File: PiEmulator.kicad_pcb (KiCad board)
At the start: 2 copper layers, 180 x 60 mm, 45 parts, among them J1 Conn_01x01, J2 Conn_01x01, J3 USB_C_Receptacle_USB2.0, U1 ADA3708, U3 BQ24090DGQ, U4 TPS61230DRCR

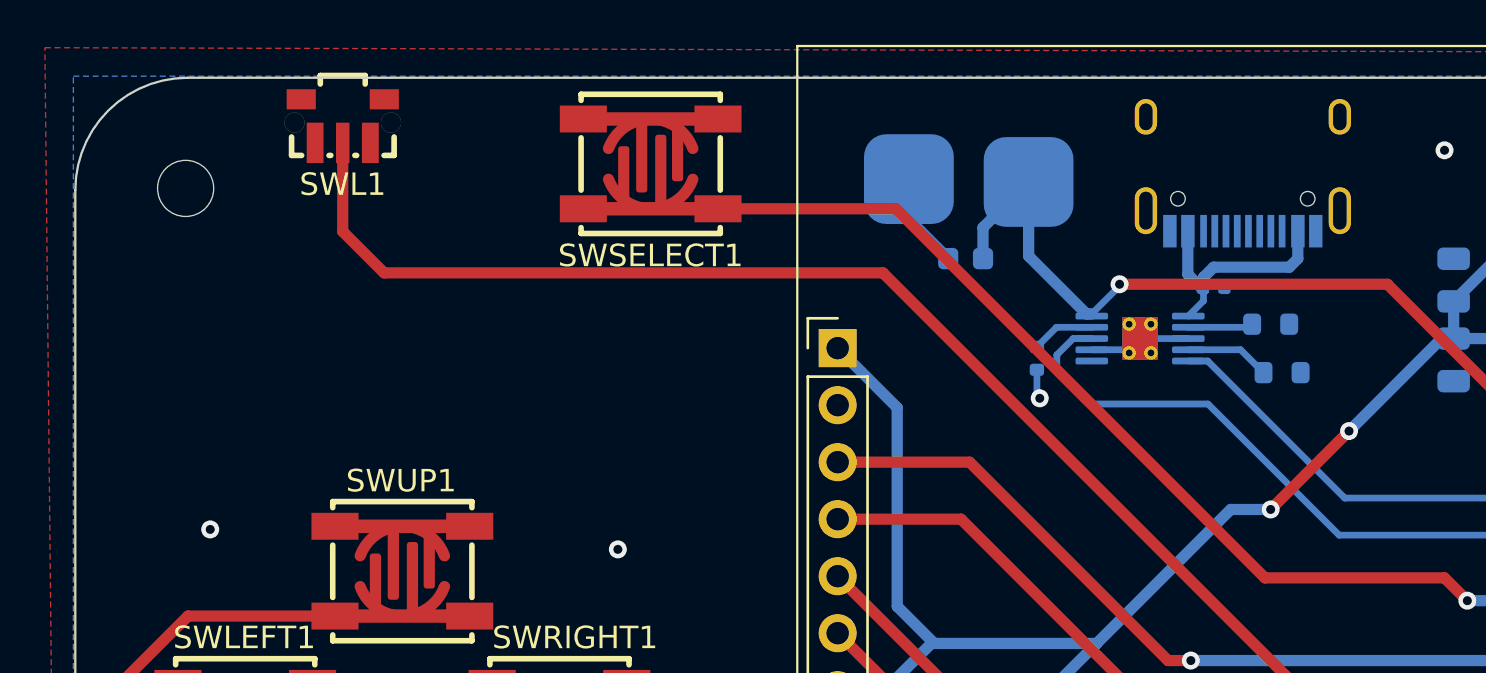
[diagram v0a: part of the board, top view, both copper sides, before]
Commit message: added jst moved usb-c
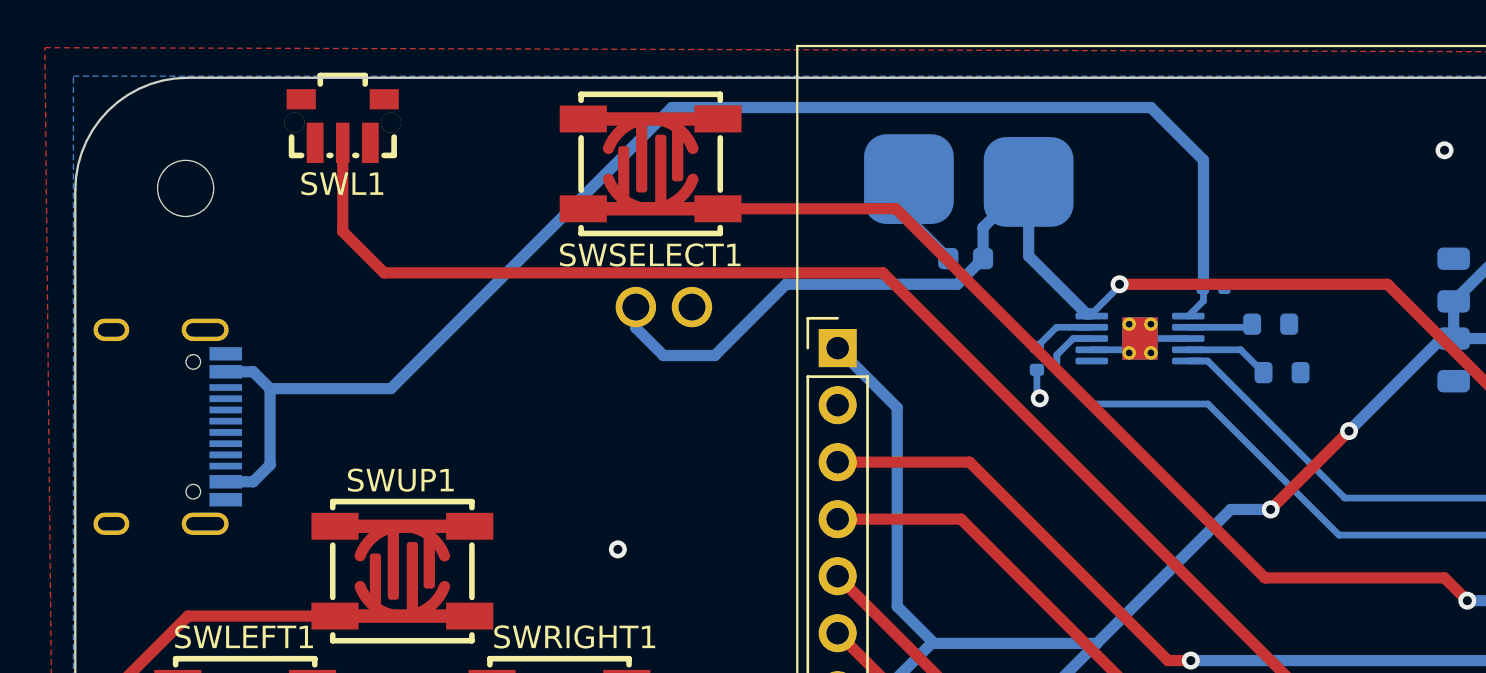
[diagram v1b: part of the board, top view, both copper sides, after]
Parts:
- added U5: XD-XH-2AW-G, easyeda2kicad:CONN-TH_2P-P2.50_XH-2AW, B.Cu at (86.6, 81.7)
- moved J3 51.0 mm to (63.1, 87.0), turned to 90 degrees
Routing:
- net VBUS: track 10.7 -> 62.9 mm
- net +BATT: track 141.2 -> 159.9 mm
- net GND: vias 19 -> 18

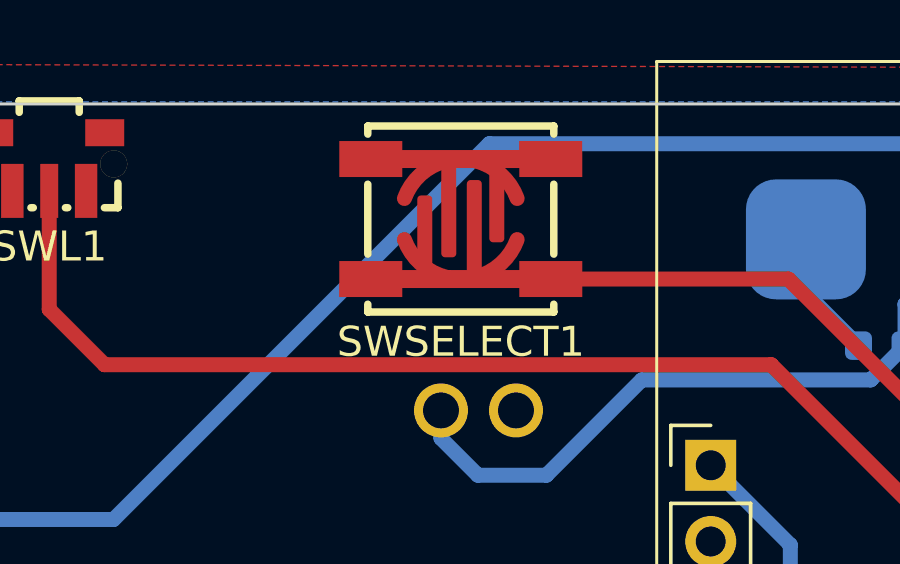
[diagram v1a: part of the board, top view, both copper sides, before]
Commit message: moved USBC, added battery connector
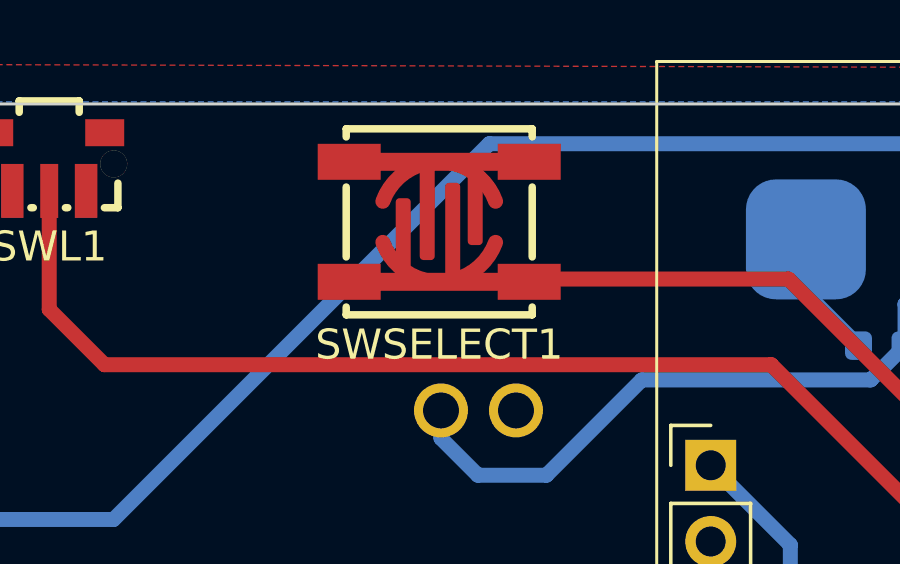
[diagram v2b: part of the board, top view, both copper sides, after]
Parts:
- moved SWSELECT1 0.72 mm to (85.3, 75.4)
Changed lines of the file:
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@@
   )
   (footprint "easyeda2kicad:SW-SMD_4P-L6.2-W6.2-P4.00-LS7.0" (layer "F.Cu")
-    (at 86.044 75.281)
+    (at 85.325 75.374)
     (property "LCSC Part" "C963191")
     (property "Sheetfile" "PiEmulator.kicad_sch")

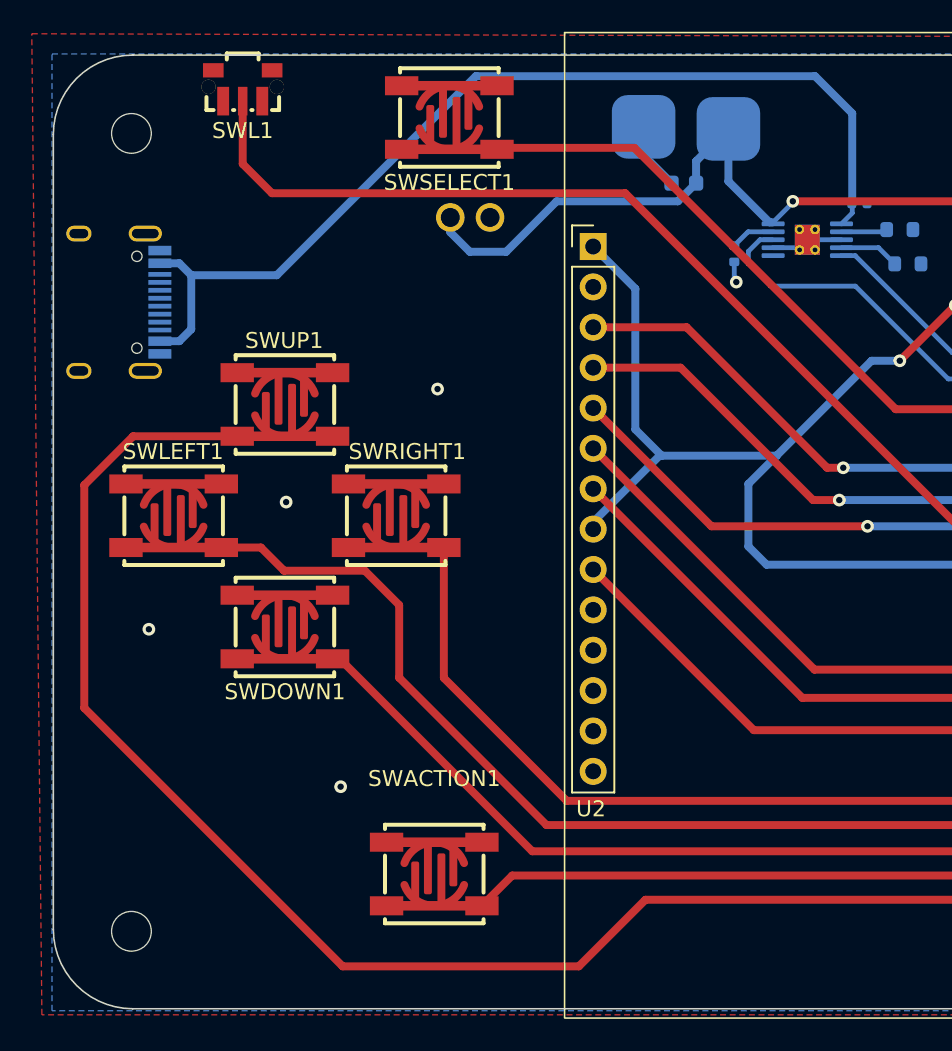
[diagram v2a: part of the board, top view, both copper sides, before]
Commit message: moved usb-c
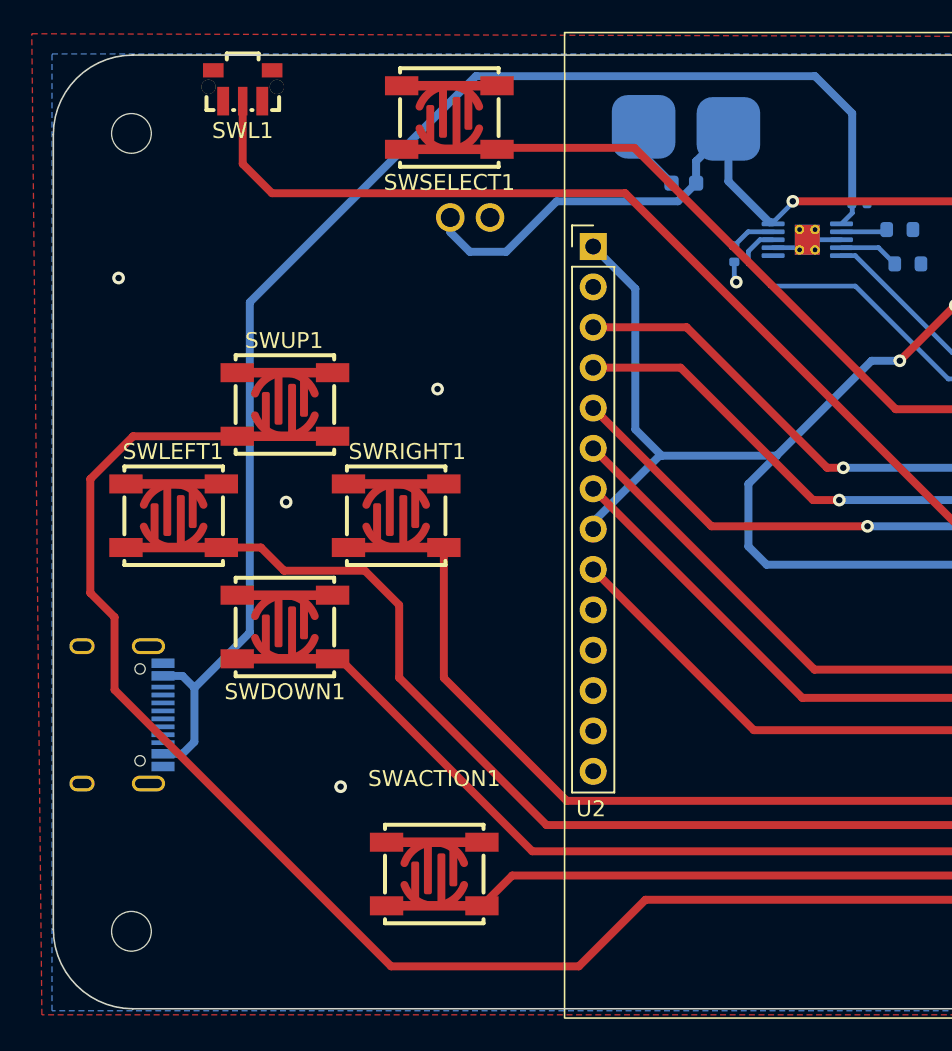
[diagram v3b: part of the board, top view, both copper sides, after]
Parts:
- moved J3 26.0 mm to (63.3, 113.0)
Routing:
- net VBUS: track 62.9 -> 85.7 mm
- net /Up: track 163.7 -> 161.6 mm
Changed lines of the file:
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@@
   )
   (footprint "Connector_USB:USB_C_Receptacle_HRO_TYPE-C-31-M-12" (layer "B.Cu")
-    (at 63.067 86.995 90)
+    (at 63.265 112.955 90)
     (descr "USB Type-C receptacle for USB 2.0 and PD, http://www.krhro.com/uploads/soft/180320/1-1P320120243.pdf")
     (tags "usb usb-c 2.0 pd")
@@
   (via (at 213.741 75.057) (size 0.8) (drill 0.4) (layers "F.Cu" "B.Cu") (free) (net 22))
   (via (at 140.462 82.931) (size 0.8) (drill 0.4) (layers "F.Cu" "B.Cu") (free) (net 22))
-  (via (at 66.421 107.569) (size 0.8) (drill 0.4) (layers "F.Cu" "B.Cu") (free) (net 22))
+  (via (at 64.516 85.471) (size 0.8) (drill 0.4) (layers "F.Cu" "B.Cu") (free) (net 22))
   (via (at 235.458 93.345) (size 0.8) (drill 0.4) (layers "F.Cu" "B.Cu") (free) (net 22))
   (via (at 223.774 105.791) (size 0.8) (drill 0.4) (layers "F.Cu" "B.Cu") (free) (net 22))
@@
   (segment (start 163.344 97.409) (end 170.197 104.262) (width 0.5) (layer "B.Cu") (net 28))
   (segment (start 110.109 97.409) (end 163.344 97.409) (width 0.5) (layer "B.Cu") (net 28))
+  (segment (start 65.43 95.427) (end 62.738 98.119) (width 0.5) (layer "F.Cu") (net 29))
+  (segment (start 64.262 106.807) (end 64.262 111.379) (width 0.5) (layer "F.Cu") (net 29))
   (segment (start 182.897 110.981) (end 182.897 106.802) (width 0.5) (layer "F.Cu") (net 29))
-  (segment (start 169.291 124.587) (end 182.897 110.981) (width 0.5) (layer "F.Cu") (net 29))
-  (segment (start 62.357 98.5) (end 62.357 112.522) (width 0.5) (layer "F.Cu") (net 29))
-  (segment (start 78.613 128.778) (end 93.472 128.778) (width 0.5) (layer "F.Cu") (net 29))
-  (segment (start 65.43 95.427) (end 62.357 98.5) (width 0.5) (layer "F.Cu") (net 29))
-  (segment (start 62.357 112.522) (end 78.613 128.778) (width 0.5) (layer "F.Cu") (net 29))
   (segment (start 71.98 95.427) (end 65.43 95.427) (width 0.5) (layer "F.Cu") (net 29))
+  (segment (start 62.738 98.119) (end 62.738 105.283) (width 0.5) (layer "F.Cu") (net 29))
+  (segment (start 64.262 111.379) (end 81.661 128.778) (width 0.5) (layer "F.Cu") (net 29))
+  (segment (start 81.661 128.778) (end 93.472 128.778) (width 0.5) (layer "F.Cu") (net 29))
+  (segment (start 62.738 105.283) (end 64.262 106.807) (width 0.5) (layer "F.Cu") (net 29))
   (segment (start 93.472 128.778) (end 97.663 124.587) (width 0.5) (layer "F.Cu") (net 29))
   (segment (start 97.663 124.587) (end 169.291 124.587) (width 0.5) (layer "F.Cu") (net 29))
+  (segment (start 169.291 124.587) (end 182.897 110.981) (width 0.5) (layer "F.Cu") (net 29))
   (segment (start 84.98 110.634) (end 92.71 118.364) (width 0.5) (layer "F.Cu") (net 30))
   (segment (start 150.114 118.364) (end 157.607 110.871) (width 0.5) (layer "F.Cu") (net 30))
@@
   (segment (start 200.787 101.854) (end 200.787 107.696) (width 0.5) (layer "B.Cu") (net 39))
   (segment (start 200.787 107.696) (end 198.374 110.109) (width 0.5) (layer "B.Cu") (net 39))
-  (segment (start 110.673 75.113) (end 110.673 80.899) (width 0.5) (layer "B.Cu") (net 40))
-  (segment (start 68.337 89.445) (end 69.088 88.694) (width 0.5) (layer "B.Cu") (net 40))
-  (segment (start 69.088 85.296) (end 74.47 85.296) (width 0.5) (layer "B.Cu") (net 40))
-  (segment (start 86.995 72.771) (end 108.331 72.771) (width 0.5) (layer "B.Cu") (net 40))
+  (segment (start 110.673 75.113) (end 108.331 72.771) (width 0.5) (layer "B.Cu") (net 40))
+  (segment (start 72.771 107.771) (end 69.286 111.256) (width 0.5) (layer "B.Cu") (net 40))
+  (segment (start 86.995 72.771) (end 72.771 86.995) (width 0.5) (layer "B.Cu") (net 40))
+  (segment (start 68.535 115.405) (end 69.286 114.654) (width 0.5) (layer "B.Cu") (net 40))
+  (segment (start 110.673 80.899) (end 110.673 75.113) (width 0.5) (layer "B.Cu") (net 40))
   (segment (start 110.673 81.386) (end 110.673 80.899) (width 0.3) (layer "B.Cu") (net 40))
-  (segment (start 68.337 84.545) (end 67.112 84.545) (width 0.5) (layer "B.Cu") (net 40))
-  (segment (start 108.331 72.771) (end 110.673 75.113) (width 0.5) (layer "B.Cu") (net 40))
-  (segment (start 67.112 89.445) (end 68.337 89.445) (width 0.5) (layer "B.Cu") (net 40))
+  (segment (start 68.535 110.505) (end 67.31 110.505) (width 0.5) (layer "B.Cu") (net 40))
+  (segment (start 67.31 115.405) (end 68.535 115.405) (width 0.5) (layer "B.Cu") (net 40))
   (segment (start 109.996 82.063) (end 110.673 81.386) (width 0.3) (layer "B.Cu") (net 40))
-  (segment (start 74.47 85.296) (end 86.995 72.771) (width 0.5) (layer "B.Cu") (net 40))
-  (segment (start 69.088 85.296) (end 68.337 84.545) (width 0.5) (layer "B.Cu") (net 40))
-  (segment (start 69.088 88.694) (end 69.088 85.296) (width 0.5) (layer "B.Cu") (net 40))
+  (segment (start 69.286 111.256) (end 68.535 110.505) (width 0.5) (layer "B.Cu") (net 40))
+  (segment (start 69.286 114.654) (end 69.286 111.256) (width 0.5) (layer "B.Cu") (net 40))
+  (segment (start 72.771 86.995) (end 72.771 107.771) (width 0.5) (layer "B.Cu") (net 40))
+  (segment (start 108.331 72.771) (end 86.995 72.771) (width 0.5) (layer "B.Cu") (net 40))
   (segment (start 109.996 82.563) (end 112.7 82.563) (width 0.3) (layer "B.Cu") (net 41))
   (segment (start 112.7 82.563) (end 112.84 82.423) (width 0.3) (layer "B.Cu") (net 41))

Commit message: added gerbers
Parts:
- added SW2: SS-12D10L5, easyeda2kicad:SW-TH_SS-12D10L5, B.Cu at (150.4, 75.6)
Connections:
- C5 pad 2: +5V -> Net-(C5-Pad2)
- C6 pad 2: +5V -> Net-(C5-Pad2)
- C7 pad 2: +5V -> Net-(C5-Pad2)
- R6 pad 1: +5V -> Net-(C5-Pad2)
- R8 pad 2: +5V -> Net-(C5-Pad2)
- U4 pad 3: +5V -> Net-(C5-Pad2)
- U4 pad 4: +5V -> Net-(C5-Pad2)
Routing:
- net Net-(C5-Pad2): track 0.00 -> 61.0 mm
- net +5V: track 115.3 -> 133.5 mm
